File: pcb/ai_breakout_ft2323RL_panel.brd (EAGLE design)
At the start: 16.3 x 25.5 mm, 14 parts, among them IC1 FT2332RL, J1 1X06LONG

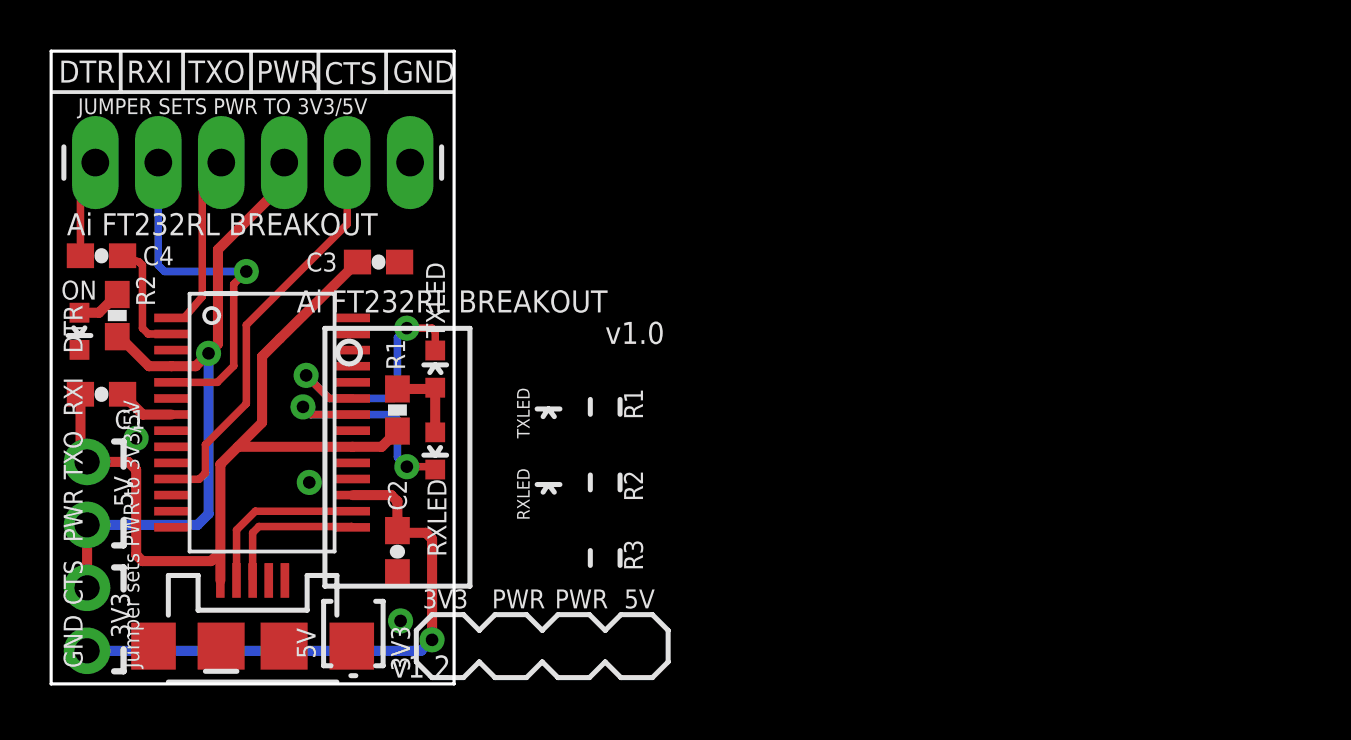
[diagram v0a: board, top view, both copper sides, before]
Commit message: New revision and adding panelized version
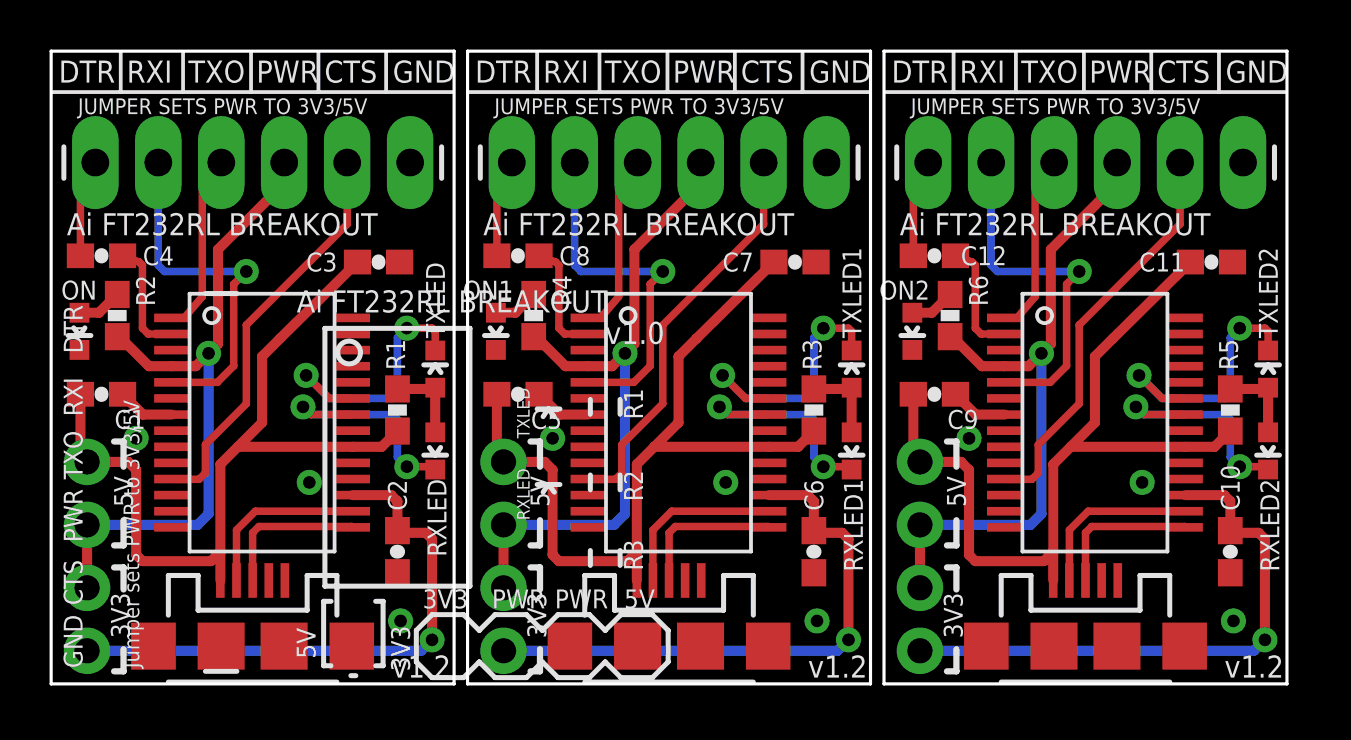
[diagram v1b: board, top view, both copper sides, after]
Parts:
- added C10, C5, C6, C9: 0.1uF, Ai_Passives:CAP-0603
- added C11, C7: 10uF, Ai_Passives:CAP-0603
- added C12, C8: 1uF, Ai_Passives:CAP-0603
- added IC2, IC3: FT2332RL, Ai_IC:SSOP28-LD
- added J2, J3: 1X06LONG, Ai_Connectors:1X06-LONG
- added JP2, JP3: 1X04NOSILK, Ai_Connectors:1X04-NOSILK
- added ON1, ON2: BLUE, Ai_LED:LED-0603
- added R3, R5: 300, Ai_Passives:RES-0603
- added R4, R6: 1K, Ai_Passives:RES-0603
- added RXLED1, RXLED2, TXLED1, TXLED2: YELLOW, Ai_LED:LED-0603
- added U$1, U$2: AI-LOGOL, Ai_Miscellany:AI-LOGO-L
- added USB2, USB3: USBMICROB, Ai_Connectors:USB-MICROB
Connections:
- new net 3V1: C6.1, IC2.17, JP2.4
- new net 3V2: C10.1, IC3.17, JP3.4
- new net 5V1: C5.1, C7.1, IC2.20, JP2.1, R3.2, USB2.VBUS
- new net 5V2: C11.1, C9.1, IC3.20, JP3.1, R5.2, USB3.VBUS
- new net CTS1: IC2.11, J2.2
- new net CTS2: IC3.11, J3.2
- new net DTR1: C8.1, IC2.2
- new net DTR2: C12.1, IC3.2
- new net GND1: C5.2, C6.2, C7.2, IC2.18, IC2.21, IC2.25, IC2.26, IC2.7, J2.1, ON1.C, USB2.GND
- new net GND2: C10.2, C11.2, C9.2, IC3.18, IC3.21, IC3.25, IC3.26, IC3.7, J3.1, ON2.C, USB3.GND
- new net N$10: R3.1, RXLED1.A, TXLED1.A
- new net N$11: ON1.A, R4.2
- new net N$12: IC2.23, TXLED1.C
- new net N$13: IC2.22, RXLED1.C
- new net N$14: C8.2, J2.6
- new net N$15: IC3.16, USB3.D-
- new net N$16: IC3.15, USB3.D+
- new net N$17: R5.1, RXLED2.A, TXLED2.A
- new net N$18: ON2.A, R6.2
- new net N$19: IC3.23, TXLED2.C
- new net N$20: IC3.22, RXLED2.C
- new net N$21: C12.2, J3.6
- new net N$8: IC2.16, USB2.D-
- new net N$9: IC2.15, USB2.D+
- new net PWR1: IC2.4, J2.3, JP2.2, JP2.3, R4.1
- new net PWR2: IC3.4, J3.3, JP3.2, JP3.3, R6.1
- new net RXI1: IC2.5, J2.5
- new net RXI2: IC3.5, J3.5
- new net TXO1: IC2.1, J2.4
- new net TXO2: IC3.1, J3.4
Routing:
- net 5V2: track 0.00 -> 33.9 mm
- net 5V1: track 0.00 -> 33.9 mm
- net PWR2: track 0.00 -> 27.5 mm, vias 0 -> 1
- net PWR1: track 0.00 -> 27.5 mm, vias 0 -> 1
- net 3V1: track 0.00 -> 22.8 mm, vias 0 -> 1
- net 3V2: track 0.00 -> 22.8 mm, vias 0 -> 1
- net CTS1: track 0.00 -> 16.4 mm
- net CTS2: track 0.00 -> 16.4 mm
- net RXI1: track 0.00 -> 14.6 mm, vias 0 -> 1
- net RXI2: track 0.00 -> 14.6 mm, vias 0 -> 1
- net N$19: track 0.00 -> 11.2 mm, vias 0 -> 2
- net N$12: track 0.00 -> 11.2 mm, vias 0 -> 2
- net N$20: track 0.00 -> 9.40 mm, vias 0 -> 2
- net N$13: track 0.00 -> 9.40 mm, vias 0 -> 2
- net TXO1: track 0.00 -> 7.37 mm
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- added copper zone on layer 1, net GND1
- added copper zone on layer 16, net GND1
- added copper zone on layer 1, net GND2
- added copper zone on layer 16, net GND2
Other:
- board size 16.3 x 25.5 mm -> 49.9 x 25.5 mm
- board text added: "C3"
- board text added: "C4"
- board text added: "ON"

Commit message: Updated BOM
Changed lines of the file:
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@@
 <setting verticaltext="up"/>
 </settings>
-<grid distance="0.1" unitdist="mm" unit="mm" style="lines" multiple="1" display="yes" altdistance="0.025" altunitdist="inch" altunit="inch"/>
+<grid distance="5" unitdist="mil" unit="mil" style="lines" multiple="1" display="yes" altdistance="0.025" altunitdist="inch" altunit="inch"/>
 <layers>
 <layer number="1" name="Top" color="4" fill="1" visible="yes" active="yes"/>
@@
 <layer number="123" name="tTestmark" color="7" fill="1" visible="yes" active="yes"/>
 <layer number="124" name="bTestmark" color="7" fill="1" visible="yes" active="yes"/>
-<layer number="125" name="_tNames" color="14" fill="1" visible="yes" active="yes"/>
-<layer number="126" name="_bNames" color="7" fill="1" visible="yes" active="yes"/>
+<layer number="125" name="_tNames" color="14" fill="1" visible="no" active="yes"/>
+<layer number="126" name="_bNames" color="7" fill="1" visible="no" active="yes"/>
 <layer number="127" name="_tValues" color="7" fill="1" visible="yes" active="yes"/>
 <layer number="128" name="_bValues" color="7" fill="1" visible="yes" active="yes"/>
@@
 <board>
 <plain>
-<wire x1="0" y1="25.527" x2="0" y2="0" width="0.127" layer="20"/>
 <wire x1="0" y1="0" x2="16.256" y2="0" width="0.127" layer="20"/>
-<wire x1="16.256" y1="0" x2="16.256" y2="25.527" width="0.127" layer="20"/>
+<wire x1="16.256" y1="0" x2="16.256" y2="25.527" width="0.127" layer="21"/>
 <wire x1="16.256" y1="25.527" x2="0" y2="25.527" width="0.127" layer="20"/>
 <text x="5.5372" y="24.257" size="0.889" layer="21" font="vector" ratio="15">TXO</text>
@@
 <text x="15.18399375" y="8.271409375" size="0.762" layer="125" ratio="15" rot="R270">RXLED</text>
 <text x="15.886403125" y="13.953590625" size="0.762" layer="125" ratio="15" rot="R90">TXLED</text>
-<wire x1="16.8" y1="25.527" x2="16.8" y2="0" width="0.127" layer="20"/>
+<wire x1="16.8" y1="25.527" x2="16.8" y2="0" width="0.127" layer="21"/>
 <wire x1="16.8" y1="0" x2="33.056" y2="0" width="0.127" layer="20"/>
-<wire x1="33.056" y1="0" x2="33.056" y2="25.527" width="0.127" layer="20"/>
+<wire x1="33.056" y1="0" x2="33.056" y2="25.527" width="0.127" layer="21"/>
 <wire x1="33.056" y1="25.527" x2="16.8" y2="25.527" width="0.127" layer="20"/>
 <text x="22.3372" y="24.257" size="0.889" layer="21" font="vector" ratio="15">TXO</text>
@@
 <text x="31.98399375" y="8.271409375" size="0.762" layer="125" ratio="15" rot="R270">RXLED</text>
 <text x="32.686403125" y="13.953590625" size="0.762" layer="125" ratio="15" rot="R90">TXLED</text>
-<wire x1="33.6" y1="25.527" x2="33.6" y2="0" width="0.127" layer="20"/>
+<wire x1="33.6" y1="25.527" x2="33.6" y2="0" width="0.127" layer="21"/>
 <wire x1="33.6" y1="0" x2="49.856" y2="0" width="0.127" layer="20"/>
 <wire x1="49.856" y1="0" x2="49.856" y2="25.527" width="0.127" layer="20"/>
@@
 <wire x1="16.528" y1="0" x2="16.528" y2="25.5" width="0.2" layer="125"/>
 <wire x1="33.328" y1="0" x2="33.328" y2="25.5" width="0.2" layer="125"/>
+<wire x1="16.256" y1="0" x2="49.911" y2="0" width="0.127" layer="20"/>
+<wire x1="49.911" y1="25.527" x2="16.256" y2="25.527" width="0.127" layer="20"/>
+<wire x1="0" y1="25.527" x2="0" y2="0" width="0.127" layer="20"/>
 </plain>
 <attributes>
